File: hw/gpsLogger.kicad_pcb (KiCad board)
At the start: 4 copper layers, 41 x 72.8 mm, 233 parts, among them IC1 MSP430F55xx, P1 USB_OTG, P2 CONN_01X02, Q2 FG6943010R, SW1 SW_PUSH, U1 MAX_M8Q, U2 MCP73812, U3 uSD, U4 MIC2091, U5 MIC2091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

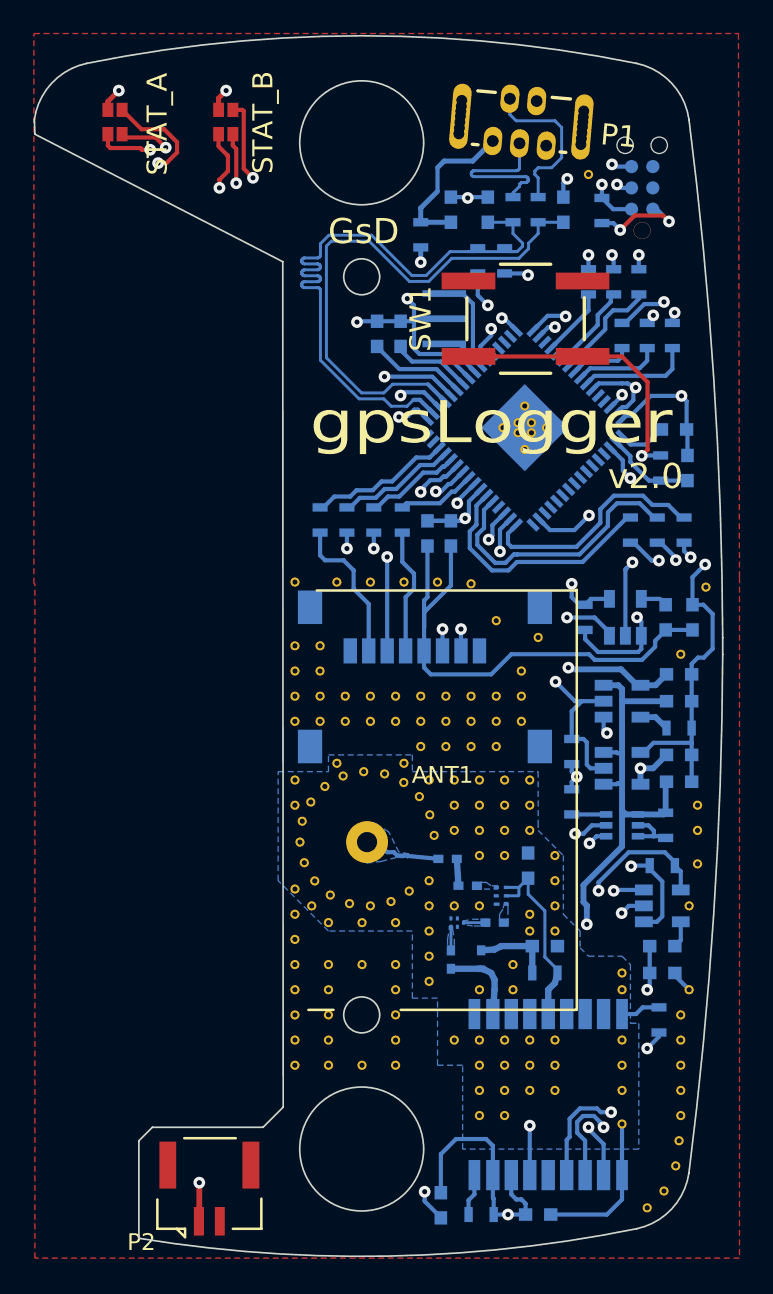
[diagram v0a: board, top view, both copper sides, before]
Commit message: Added small link connecting ground pads.
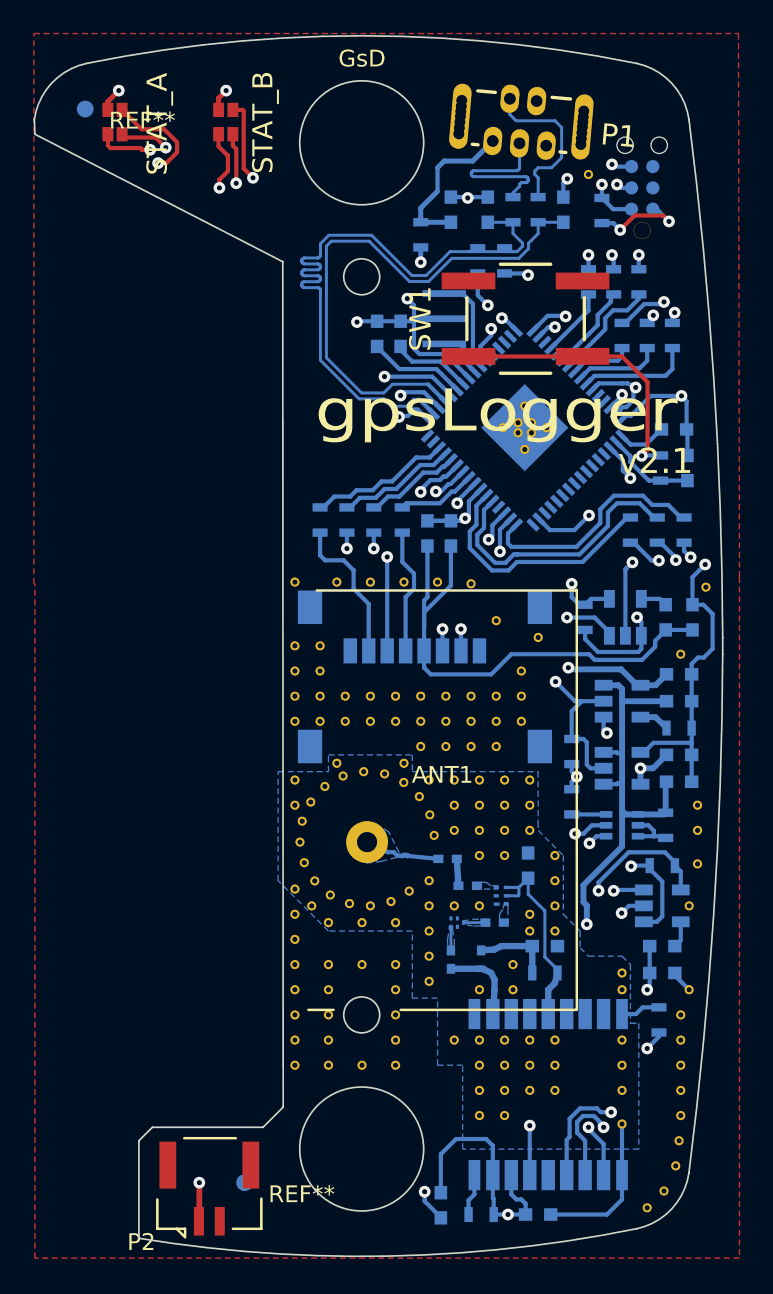
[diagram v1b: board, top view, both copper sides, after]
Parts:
- added REF**: Fiducial_1mm_Dia_2.54mm_Outer_CopperBottom, Fiducials:Fiducial_1mm_Dia_2.54mm_Outer_CopperBottom, F.Cu at (144.5, 134.5)
- added REF**: Fiducial_1mm_Dia_2.54mm_Outer_CopperBottom, Fiducials:Fiducial_1mm_Dia_2.54mm_Outer_CopperBottom, F.Cu at (135.0, 70.5)
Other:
- board text added: "v2.1"
- board text removed: "v2.0"
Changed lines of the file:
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@@
 (kicad_pcb (version 4) (host pcbnew 4.0.2-stable)
   (general
-    (links 200)
-    (no_connects 72)
+    (links 0)
+    (no_connects 1)
     (area -81.418183 56.392421 173.050002 148.634556)
     (thickness 1.6)
@@
     (tracks 1093)
     (zones 0)
-    (modules 233)
+    (modules 235)
     (nets 103)
   )
@@
     (visible_elements 7FFCFF7F)
     (pcbplotparams
-      (layerselection 0x01030_80000001)
+      (layerselection 0x010fc_80000007)
       (usegerberextensions true)
       (excludeedgelayer true)
@@
       (drillshape 0)
       (scaleselection 1)
-      (outputdirectory ""))
+      (outputdirectory gerber/))
   )
   (net 0 "")
@@
     (add_net /USB_IN_P)
   )
+  (module Fiducials:Fiducial_1mm_Dia_2.54mm_Outer_CopperBottom (layer F.Cu)
+    (at 144.5 134.5)
+    (descr "Circular Fiducial, 1mm bare copper bottom; 2.54mm keepout")
+    (tags marker)
+    (attr virtual)
+    (fp_text reference REF** (at 3.4 0.7) (layer F.SilkS)
+      (effects (font (size 1 1) (thickness 0.15)))
+    )
+    (fp_text value Fiducial_1mm_Dia_2.54mm_Outer_CopperBottom (at 0 -1.8) (layer F.Fab)
+      (effects (font (size 1 1) (thickness 0.15)))
+    )
+    (fp_circle (center 0 0) (end 1.55 0) (layer B.CrtYd) (width 0.05))
+    (pad ~ smd circle (at 0 0) (size 1 1) (layers B.Cu B.Mask)
+      (solder_mask_margin 0.77) (clearance 0.77))
+  )
   (module Wire_Pads:SolderWirePad_single_0-8mmDrill (layer F.Cu)
     (at 160.8 89.8)
@@
     )
   )
+  (module Fiducials:Fiducial_1mm_Dia_2.54mm_Outer_CopperBottom (layer F.Cu)
+    (at 135 70.5)
+    (descr "Circular Fiducial, 1mm bare copper bottom; 2.54mm keepout")
+    (tags marker)
+    (attr virtual)
+    (fp_text reference REF** (at 3.4 0.7) (layer F.SilkS)
+      (effects (font (size 1 1) (thickness 0.15)))
+    )
+    (fp_text value Fiducial_1mm_Dia_2.54mm_Outer_CopperBottom (at 0 -1.8) (layer F.Fab)
+      (effects (font (size 1 1) (thickness 0.15)))
+    )
+    (fp_circle (center 0 0) (end 1.55 0) (layer B.CrtYd) (width 0.05))
+    (pad ~ smd circle (at 0 0) (size 1 1) (layers B.Cu B.Mask)
+      (solder_mask_margin 0.77) (clearance 0.77))
+  )
   (gr_line (start 138.2 132) (end 138.197341 137.816295) (layer Edge.Cuts) (width 0.1))
   (gr_line (start 139 131.2) (end 138.2 132) (layer Edge.Cuts) (width 0.1))
   (gr_line (start 145.6 131.2) (end 139 131.2) (layer Edge.Cuts) (width 0.1))
   (gr_line (start 146.8 130) (end 145.6 131.2) (layer Edge.Cuts) (width 0.1))
-  (gr_text v2.0 (at 168.4 92.4) (layer F.SilkS)
+  (gr_text "v2.1\n" (at 169 91.5) (layer F.SilkS)
     (effects (font (size 1.5 1.5) (thickness 0.2)))
   )
-  (gr_text gpsLogger (at 159.2 89.2) (layer F.SilkS)
+  (gr_text gpsLogger (at 159.5 88.5) (layer F.SilkS)
     (effects (font (size 2.5 3) (thickness 0.2)))
   )
@@
     (effects (font (size 1.2 1.2) (thickness 0.2)))
   )
-  (gr_text GsD (at 151.6 77.8) (layer F.SilkS)
-    (effects (font (size 1.5 1.5) (thickness 0.3)))
+  (gr_text GsD (at 151.5 67.5) (layer F.SilkS)
+    (effects (font (size 1 1) (thickness 0.18)))
   )
   (gr_circle (center 151.480119 132.513078) (end 147.786348 132.513078) (layer Cmts.User) (width 0.1))
@@
     (min_thickness 0.15)
     (keepout (tracks allowed) (vias allowed) (copperpour not_allowed))
-    (fill yes (arc_segments 32) (thermal_gap 0.17) (thermal_bridge_width 0.17) (smoothing fillet) (radius 0.8))
+    (fill yes (arc_segments 32) (thermal_gap 0.17) (thermal_bridge_width 0.17))
     (polygon
       (pts
@@
     (min_thickness 0.15)
     (keepout (tracks allowed) (vias allowed) (copperpour not_allowed))
-    (fill yes (arc_segments 32) (thermal_gap 0.17) (thermal_bridge_width 0.17) (smoothing fillet) (radius 0.8))
+    (fill yes (arc_segments 32) (thermal_gap 0.17) (thermal_bridge_width 0.17))
     (polygon
       (pts
-        (xy 146.4 98.4) (xy 171.4 98.4) (xy 171.4 98) (xy 146.4 98)
+        (xy 148 98.4) (xy 171.4 98.4) (xy 171.4 98) (xy 148 98)
       )
     )
@@
     (min_thickness 0.15)
     (keepout (tracks allowed) (vias allowed) (copperpour not_allowed))
-    (fill yes (arc_segments 32) (thermal_gap 0.17) (thermal_bridge_width 0.17) (smoothing fillet) (radius 0.8))
+    (fill yes (arc_segments 32) (thermal_gap 0.17) (thermal_bridge_width 0.17))
     (polygon
       (pts
